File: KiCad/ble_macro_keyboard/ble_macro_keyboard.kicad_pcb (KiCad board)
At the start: 2 copper layers, 88 x 95.5 mm, 41 parts, among them IC1 ADP3338AKCZ-3.3-RL, J1 Conn_01x03_Male, Q1 IRLML6402, SW1 SW_SPDT, SW10 SW_Push, SW11 SW_Push, SW12 SW_Push, SW13 SW_Push, SW14 SW_Push, SW2 SW_Push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

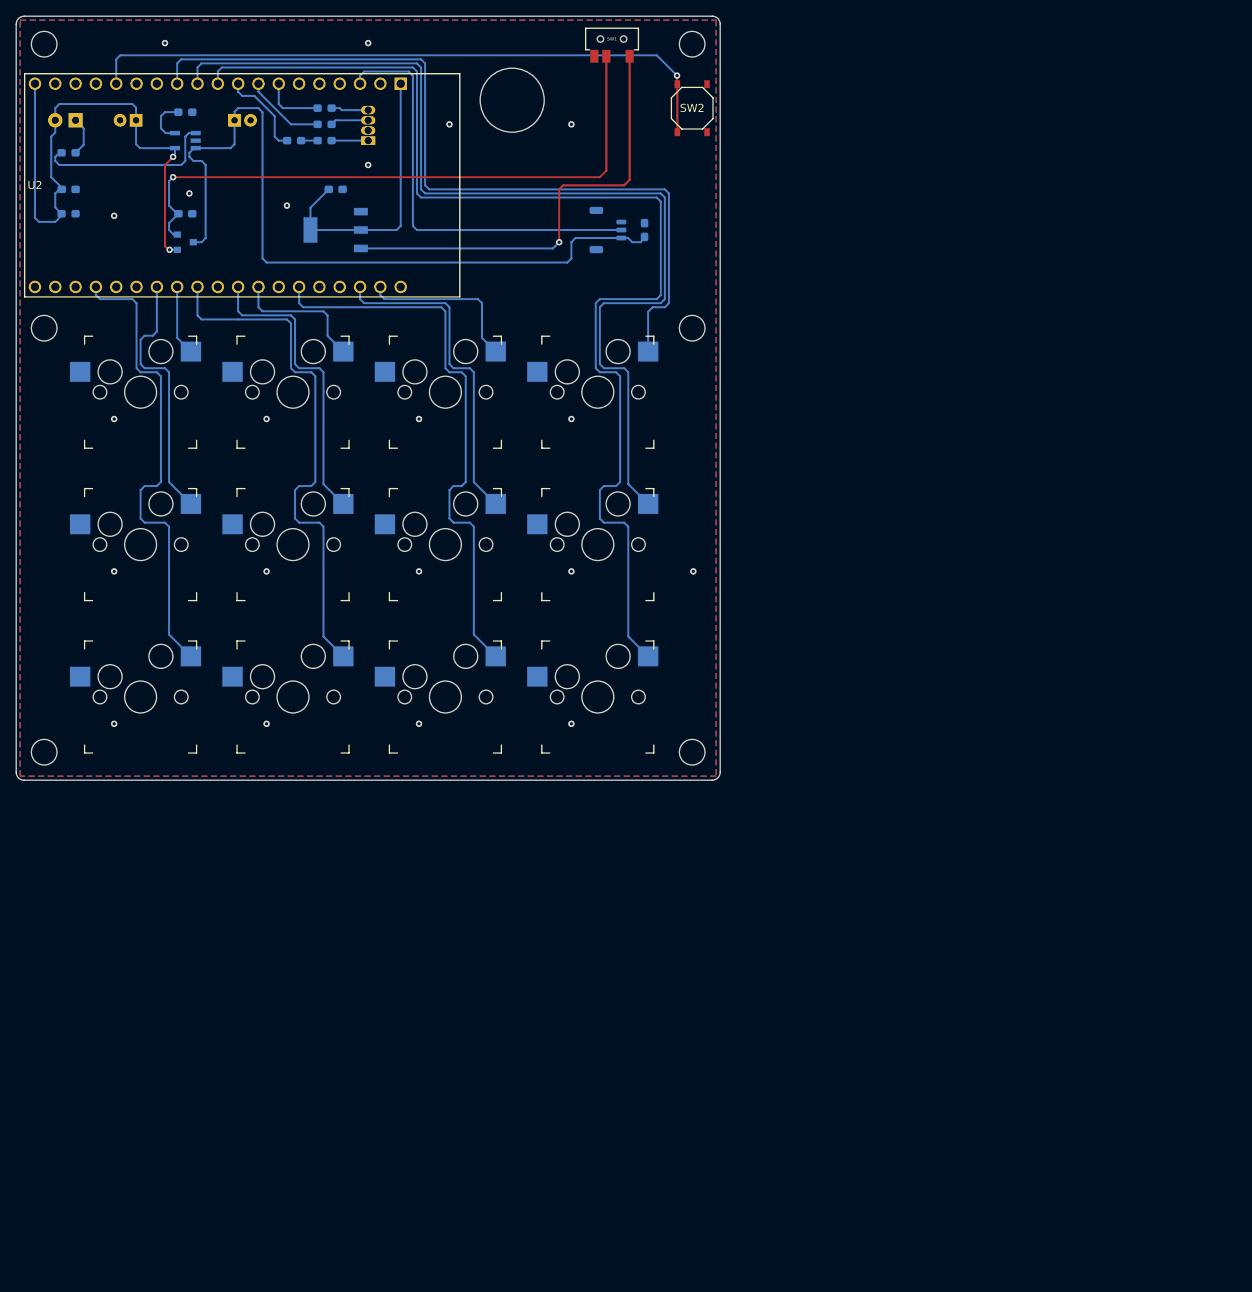
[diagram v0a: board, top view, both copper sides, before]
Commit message: [fix] User.drawingsレイヤーに底板のアクリルプレート、User.Eco1にキースイッチプレートのアクリルの図面を設定
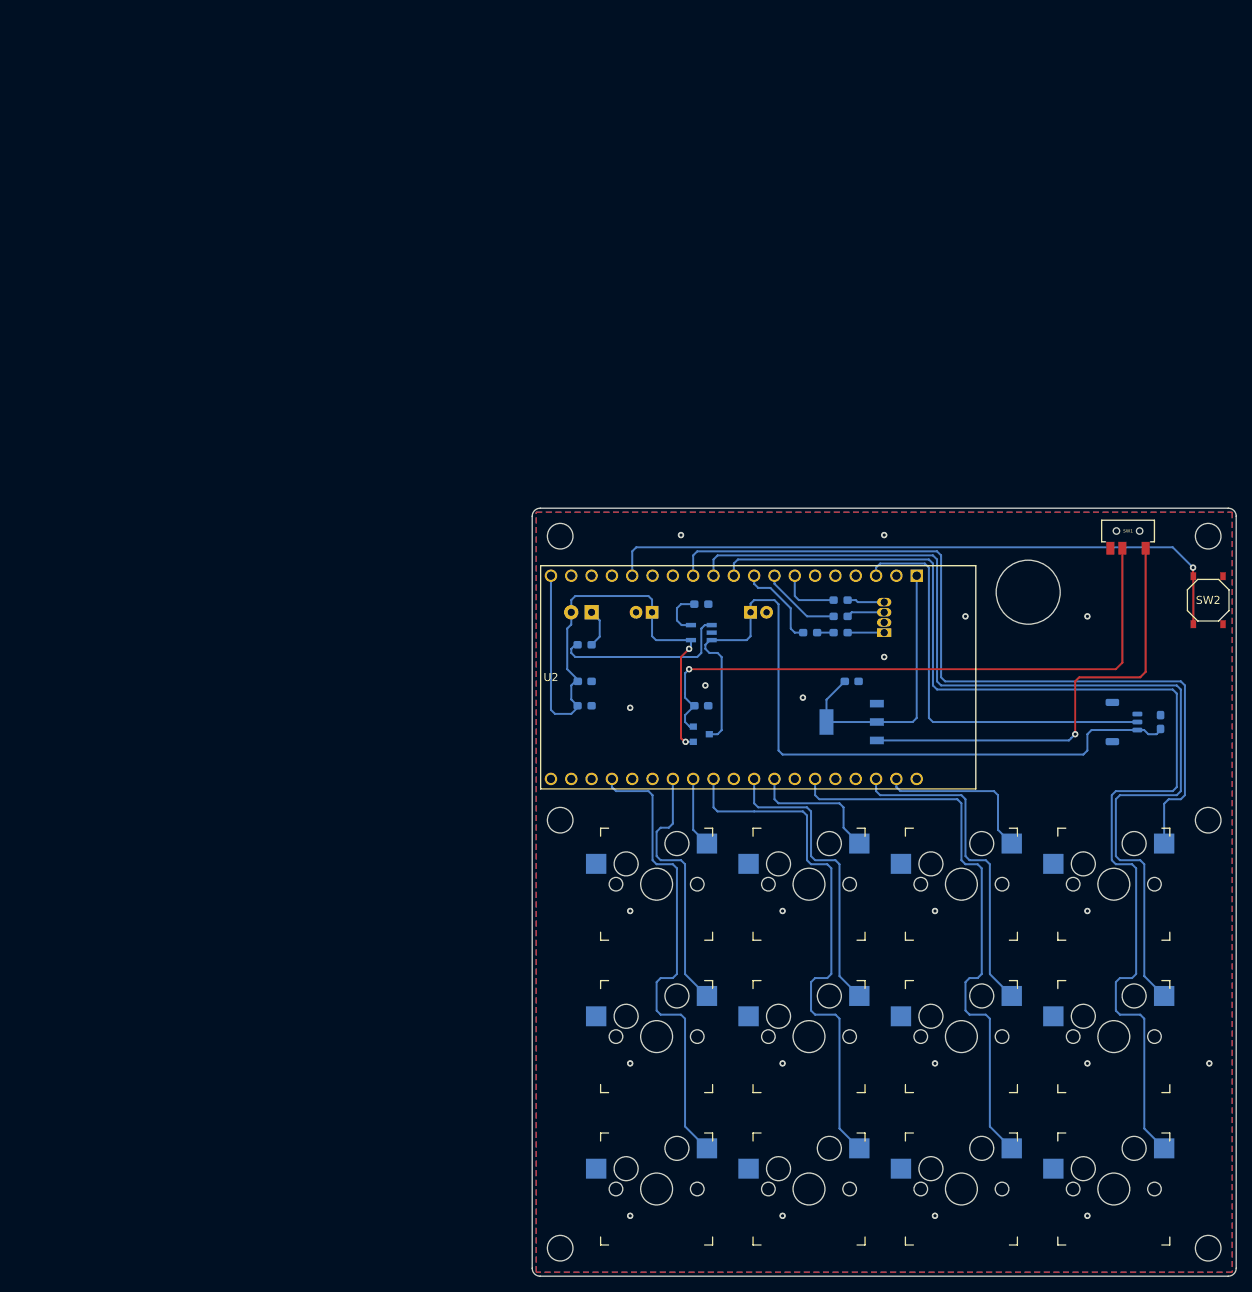
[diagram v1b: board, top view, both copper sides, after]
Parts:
- moved REF** 89.5 mm to (24.0, 110.0)
- moved REF** 89.5 mm to (105.0, 110.0)
- moved C1 89.1 mm to (27.1, 39.1)
- moved C2 89.1 mm to (99.0, 44.2)
- moved C3 89.1 mm to (41.6, 42.2)
- moved C4 89.1 mm to (60.4, 39.1)
- moved C5 89.1 mm to (35.5, 30.5)
- moved C6 89.1 mm to (47.8, 30.5)
- moved D1 89.1 mm to (27.9, 30.5)
- moved D2 89.1 mm to (64.5, 33.1)
- moved IC1 89.1 mm to (60.4, 44.2)
- moved J1 89.1 mm to (94.5, 44.2)
- moved Q1 89.1 mm to (41.6, 45.8)
- moved R1 89.1 mm to (59.1, 29.0)
- moved R2 89.1 mm to (59.1, 31.0)
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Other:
- board size 88 x 95.5 mm -> 88 x 96 mm
